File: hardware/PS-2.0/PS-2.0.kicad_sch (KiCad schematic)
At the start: 51 parts, among them J1 PinSocket_02x16_P2.54mm_Verti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, J2 Conn_01x05, J3 Conn_01x05, J8 Conn_01x03, J9 Conn_01x03, K1 RAYEX-L90, K2 RAYEX-L90, Q1 IRFPE50, Q2 IRFPE50, Q3 IRFPE50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

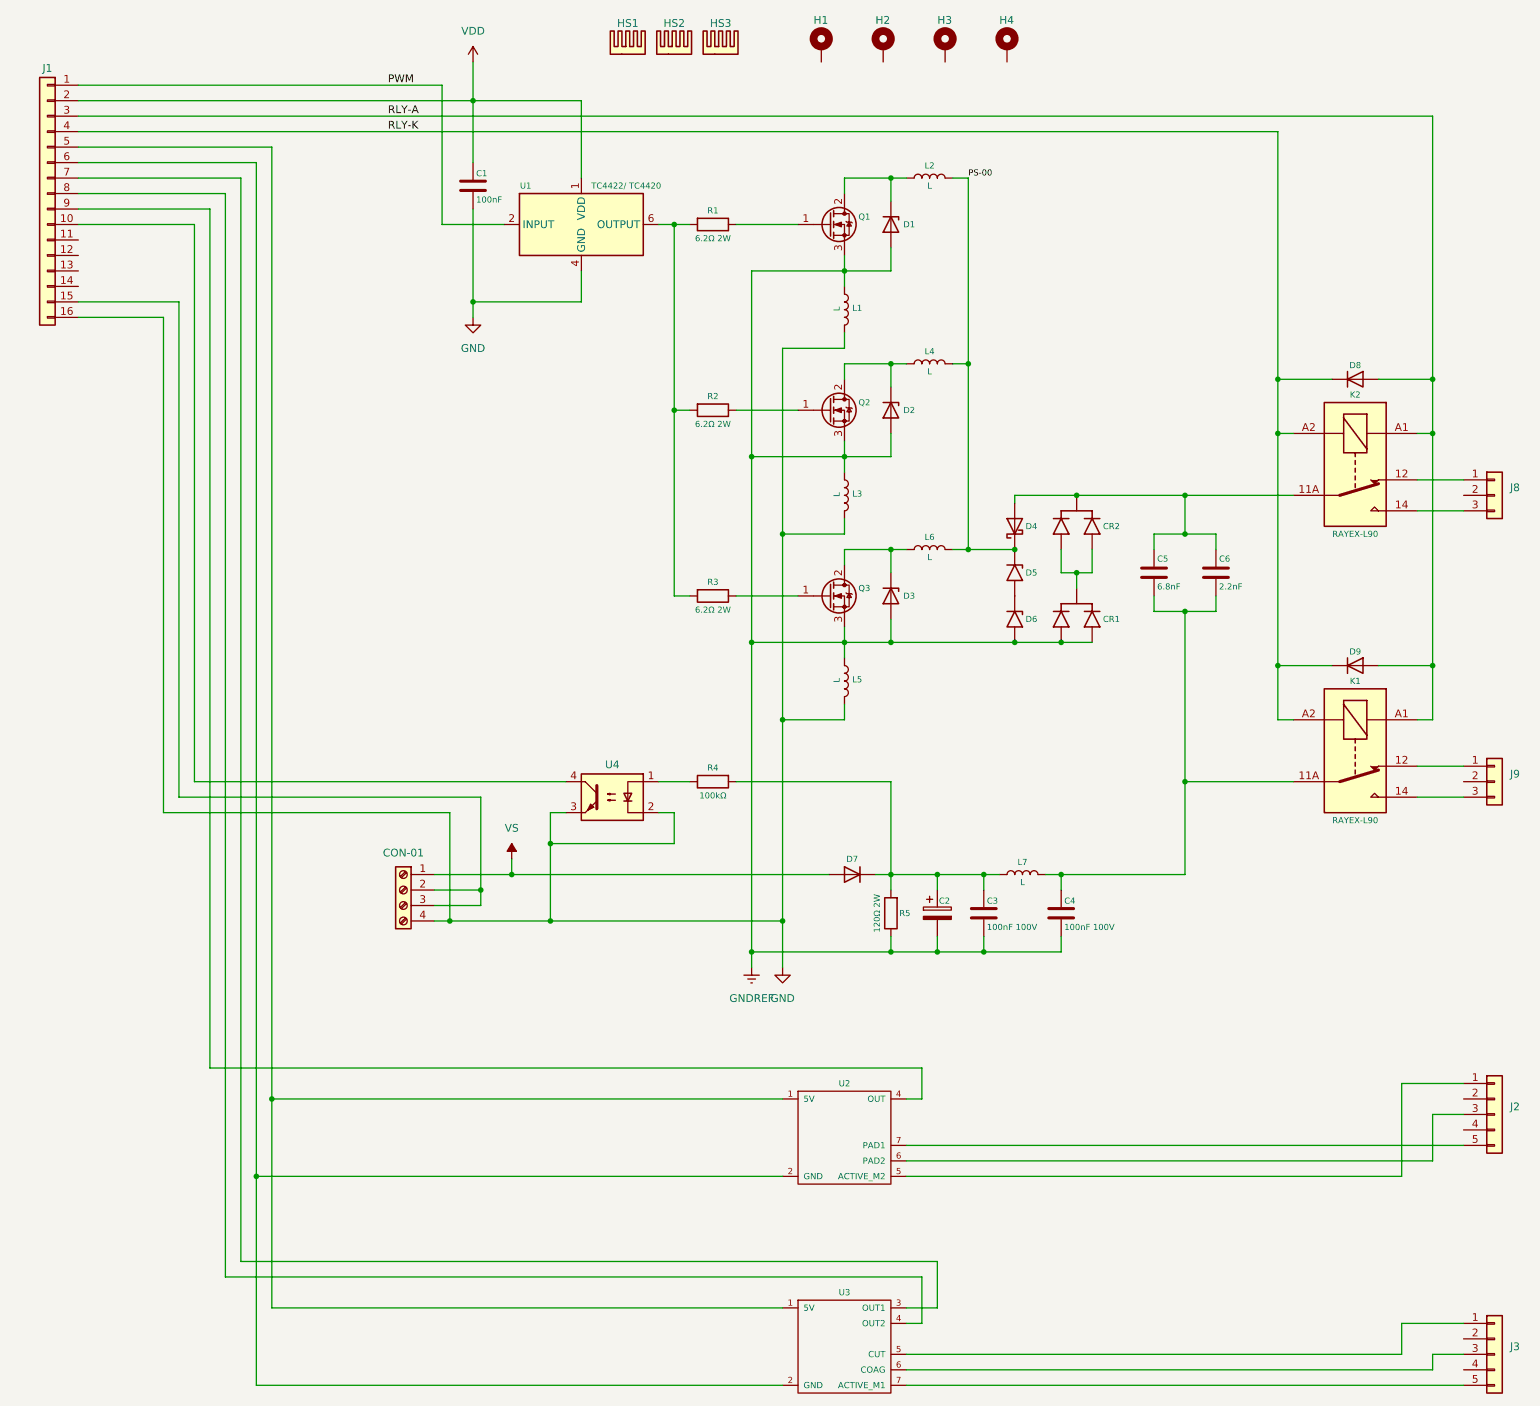
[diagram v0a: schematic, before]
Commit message: modified:   .DS_Store 	new file:   hardware/CTL-1.0/CTL-1.0-backups/CTL-1.0-2025-05-23_140814.zip 	new file:   hardware/CTL-1.0/CTL-1.0-backups/CTL-1.0-2025-05-23_142136.zip 	new file:   hardware/CTL-1.0/CTL-1.0-backups/CTL-1.0-2025-05-23_145207.zip 	new file:   hardware/CTL-1.0/CTL-1.0-backups/CTL-1.0-2025-05-23_145749.zip 	new file:   hardware/CTL-1.0/CTL-1.0-backups/CTL-1.0-2025-05-27_175205.zip 	new file:   hardware/CTL-1.0/CTL-1.0-backups/CTL-1.0-2025-05-27_180035.zip 	new file:   hardware/CTL-1.0/CTL-1.0-backups/CTL-1.0-2025-05-27_181441.zip 	new file:   hardware/CTL-1.0/CTL-1.0-backups/CTL-1.0-2025-05-27_182529.zip 	new file:   hardware/CTL-1.0/CTL-1.0-backups/CTL-1.0-2025-05-27_183819.zip 	new file:   hardware/CTL-1.0/CTL-1.0-backups/CTL-1.0-2025-05-28_201558.zip 	new file:   hardware/CTL-1.0/CTL-1.0-backups/CTL-1.0-2025-05-28_202523.zip 	new file:   hardware/CTL-1.0/CTL-1.0-backups/CTL-1.0-2025-05-28_203223.zip 	new file:   hardware/CTL-1.0/CTL-1.0-backups/CTL-1.0-2025-05-28_203806.zip 	new file:   hardware/CTL-1.0/CTL-1.0-backups/CTL-1.0-2025-05-28_204313.zip 	new file:   hardware/CTL-1.0/CTL-1.0-backups/CTL-1.0-2025-05-30_173028.zip 	new file:   hardware/CTL-1.0/CTL-1.0-backups/CTL-1.0-2025-05-30_174116.zip 	new file:   hardware/CTL-1.0/CTL-1.0-backups/CTL-1.0-2025-05-30_175122.zip 	new file:   hardware/CTL-1.0/CTL-1.0-backups/CTL-1.0-2025-05-30_180325.zip 	new file:   hardware/CTL-1.0/CTL-1.0-backups/CTL-1.0-2025-05-30_180909.zip 	new file:   hardware/CTL-1.0/CTL-1.0-backups/CTL-1.0-2025-06-03_185115.zip 	new file:   hardware/CTL-1.0/CTL-1.0-backups/CTL-1.0-2025-06-03_190157.zip 	new file:   hardware/CTL-1.0/CTL-1.0-backups/CTL-1.0-2025-06-03_222127.zip 	new file:   hardware/CTL-1.0/CTL-1.0-backups/CTL-1.0-2025-06-03_222647.zip 	new file:   hardware/CTL-1.0/CTL-1.0-backups/CTL-1.0-2025-06-03_223358.zip 	new file:   hardware/CTL-1.0/CTL-1.0-backups/CTL-1.0-2025-06-03_223905.zip 	modified:   hardware/CTL-1.0/CTL-1.0.kicad_pcb 	new file:   hardware/CTL-1.0/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
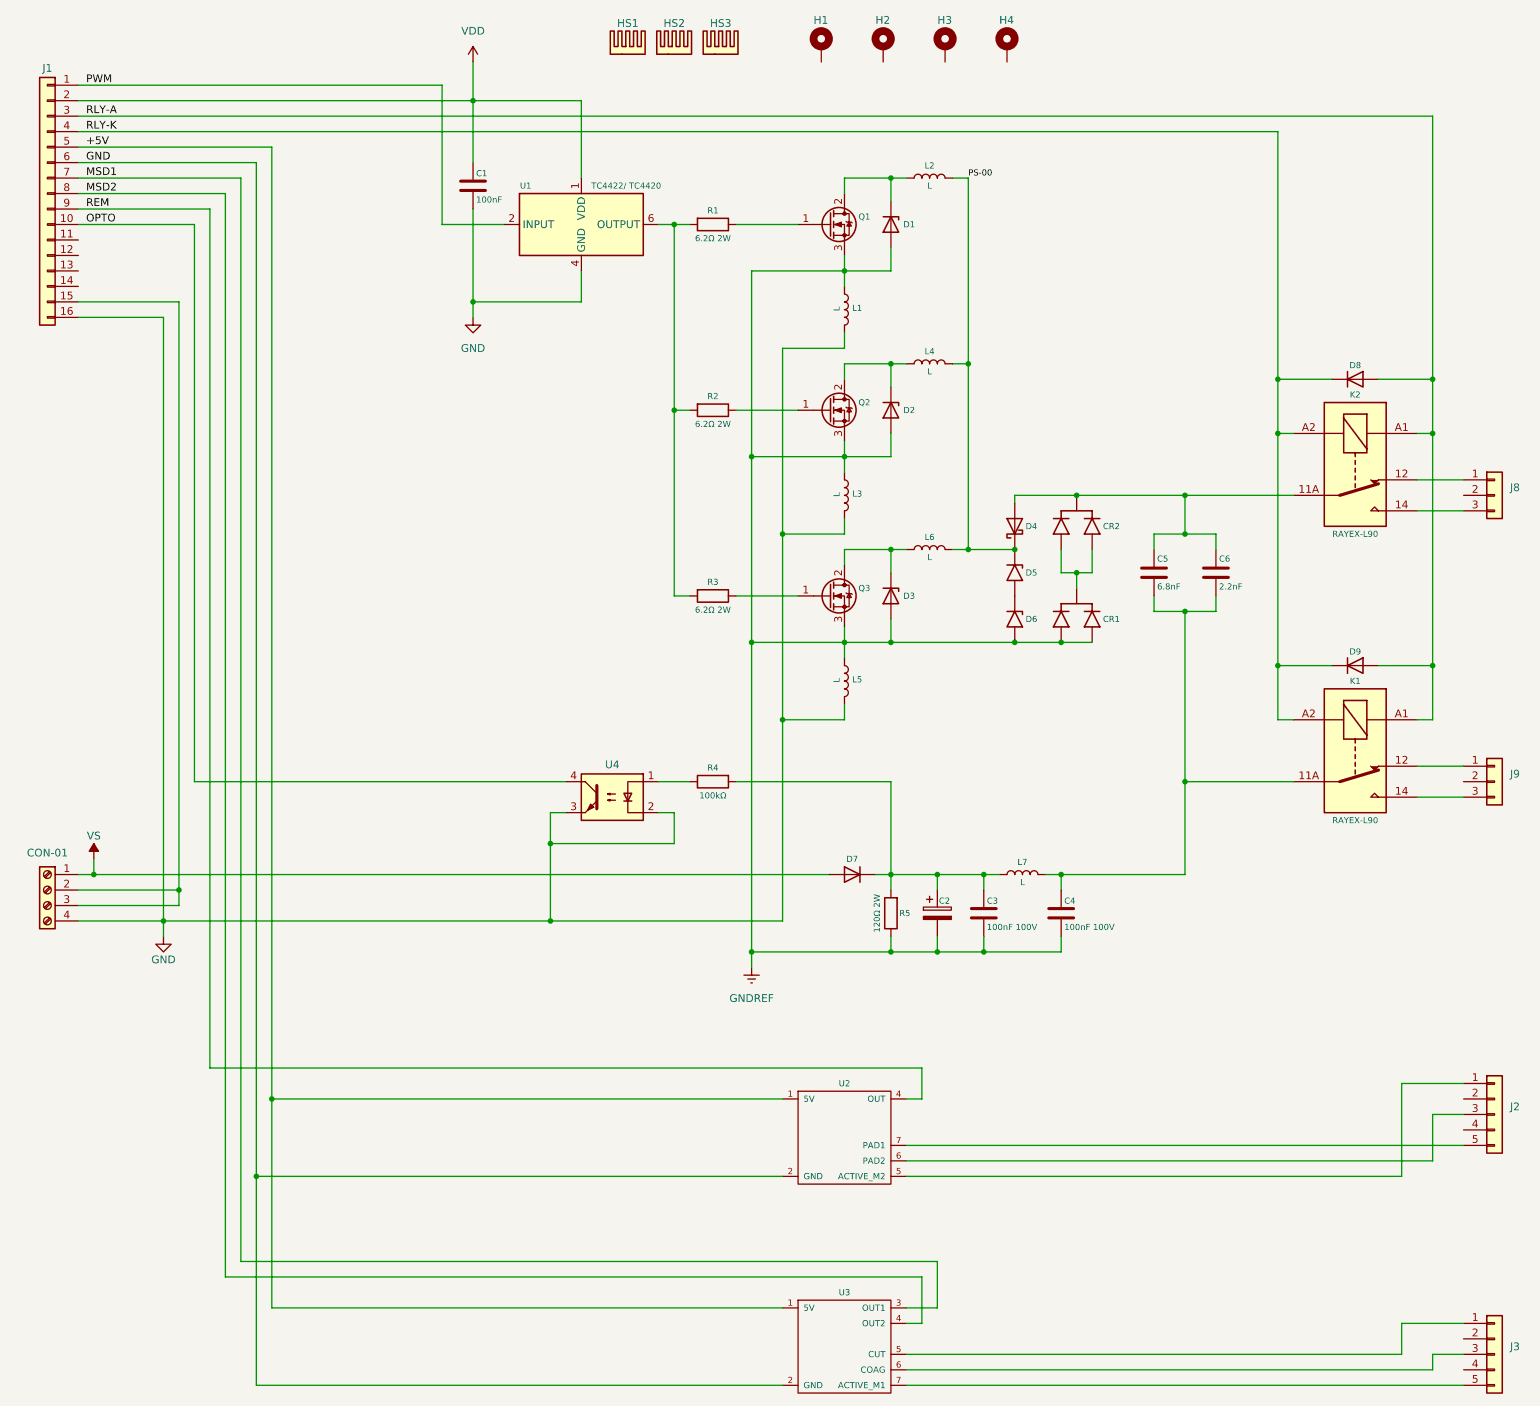
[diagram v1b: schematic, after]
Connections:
- net GND: now also J1.6 (Pin_6), U2.2 (GND), U3.2 (GND)
- net OPTO: now reaches J1.10 (Pin_10), U4.4
- net +5V: now reaches J1.5 (Pin_5), U2.1 (5V), U3.1 (5V)
- net MSD1: now reaches J1.7 (Pin_7), U3.3 (OUT1)
- net MSD2: now reaches J1.8 (Pin_8), U3.4 (OUT2)
- net REM: now reaches J1.9 (Pin_9), U2.4 (OUT)
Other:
- moved on the sheet: CON-01

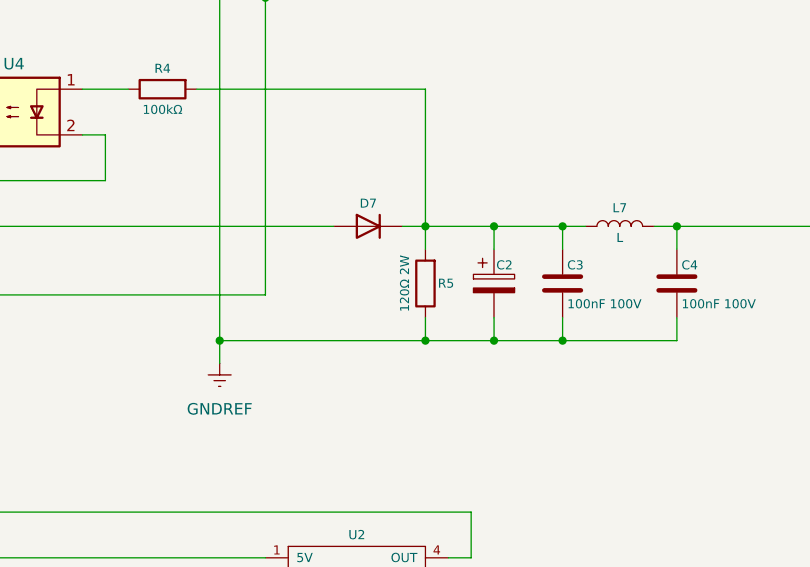
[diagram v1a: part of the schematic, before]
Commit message: modified:   .DS_Store 	modified:   README.md 	deleted:    hardware/CTL-1.0/CTL-1.0-backups/CTL-1.0-2025-05-23_140814.zip 	deleted:    hardware/CTL-1.0/CTL-1.0-backups/CTL-1.0-2025-05-23_142136.zip 	deleted:    hardware/CTL-1.0/CTL-1.0-backups/CTL-1.0-2025-05-23_145207.zip 	deleted:    hardware/CTL-1.0/CTL-1.0-backups/CTL-1.0-2025-05-23_145749.zip 	deleted:    hardware/CTL-1.0/CTL-1.0-backups/CTL-1.0-2025-06-03_185115.zip 	new file:   hardware/CTL-1.0/CTL-1.0-backups/CTL-1.0-2025-06-04_091843.zip 	new file:   hardware/CTL-1.0/CTL-1.0-backups/CTL-1.0-2025-06-04_105408.zip 	new file:   hardware/CTL-1.0/CTL-1.0-backups/CTL-1.0-2025-06-04_105918.zip 	new file:   hardware/CTL-1.0/CTL-1.0-backups/CTL-1.0-2025-06-04_110436.zip 	new file:   hardware/CTL-1.0/CTL-1.0-backups/CTL-1.0-2025-06-04_115049.zip 	new file:   hardware/CTL-1.0/CTL-1.0-backups/CTL-1.0-2025-06-04_132910.zip 	modified:   hardware/CTL-1.0/CTL-1.0.kicad_pcb 	modified:   hardware/CTL-1.0/CTL-1.0.kicad_prl 	modified:   hardware/CTL-1.0/CTL-1.0.kicad_sch 	new file:   hardware/PS-2.0/PS-2.0-backups/PS-2.0-2025-06-04_100004.zip 	new file:   hardware/PS-2.0/PS-2.0-backups/PS-2.0-2025-06-04_102434.zip 	new file:   hardware/PS-2.0/PS-2.0-backups/PS-2.0-2025-06-04_104734.zip 	new file:   hardware/PS-2.0/PS-2.0-backups/PS-2.0-2025-06-04_133345.zip 	modified:   hardware/PS-2.0/PS-2.0.kicad_pcb 	modified:   hardware/PS-2.0/PS-2.0.kicad_prl 	modified:   hardware/PS-2.0/PS-2.0.kicad_sch 	new file:   hardware/PS-2.0/~PS-2.0.kicad_pcb.lck 	new file:   hardware/PS-2.0/~PS-2.0.kicad_sch.lck 	modified:   pic/.DS_Store 	new file:   pic/PWM/Wave-pure-cut-driver-mosfet.png 	renamed:    pic/PWM/blend-cut-1/blend-cut-1-10.csv -> pic/PWM/blend-cut-1/CTL/blend-cut-1-10.csv 	renamed:    pic/PWM/blend-cut-1/blend-cut-1-10.png -> pic/PWM/blend-cut-1/CTL/blend-cut-1-10.png 	renamed:    pic/PWM/blend-cut-1/blend-cut-1-100.csv -> pic/PWM/blend-cut-1/CTL/blend-cut-1-100.csv 	renamed:    pic/PWM/blend-cut-1/blend-cut-1-100.png -> pic/PWM/ble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
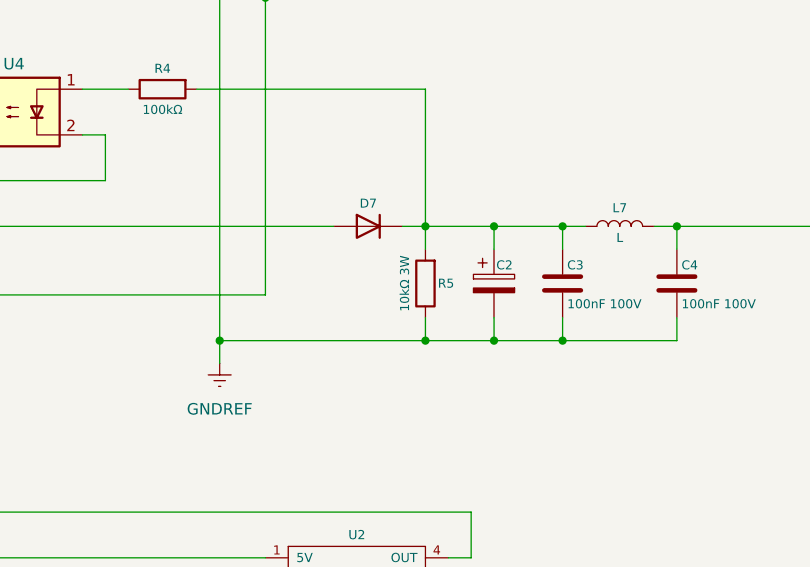
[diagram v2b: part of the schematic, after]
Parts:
- R5: value 120Ω 2W -> 10kΩ 3W
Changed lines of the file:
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@@
 			)
 		)
-		(property "Value" "120Ω 2W"
+		(property "Value" "10kΩ 3W"
 			(at 165.354 184.15 90)
 			(effects
